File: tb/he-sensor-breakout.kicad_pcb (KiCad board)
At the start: 2 copper layers, 19 x 19 mm, 24 parts, among them J1 Conn_01x01_Pin, J10 Conn_01x01_Pin, J11 Conn_01x01_Pin, J12 Conn_01x01_Pin, J13 Conn_01x01_Pin, J14 Conn_01x01_Pin, J2 Conn_01x01_Pin, J3 Conn_01x01_Pin, J4 Conn_01x01_Pin, J5 Conn_01x01_Pin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

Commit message: adds panelization tabs
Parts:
- added REF**: Tab, kikit:Tab, F.Cu at (116.0, 107.8)
- added REF**: Tab, kikit:Tab, F.Cu at (111.0, 92.0)
- added REF**: Tab, kikit:Tab, F.Cu at (101.0, 114.0)
- added REF**: Tab, kikit:Tab, F.Cu at (111.0, 114.0)
- added REF**: Tab, kikit:Tab, F.Cu at (101.0, 92.0)
- added REF**: Tab, kikit:Tab, F.Cu at (116.0, 98.4)
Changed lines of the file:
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@@
     )
+  )
+  (footprint "kikit:Tab" (layer "F.Cu")
+    (at 116 107.7875 180)
+    (descr "A symbol representing annotation for tab placement")
+    (attr exclude_from_pos_files exclude_from_bom)
+    (fp_text reference "REF**" (at 0 -2) (layer "F.SilkS") hide
+        (effects (font (size 1 1) (thickness 0.15)))
+    )
+    (fp_text value "Tab" (at -3 -1) (layer "Dwgs.User")
+        (effects (font (size 1.2 1.2) (thickness 0.2)))
+    )
+    (fp_text user "KIKIT: width: 7mm" (at -5.5 0 90) (layer "Dwgs.User")
+        (effects (font (size 1 1) (thickness 0.15)))
+    )
+    (fp_line (start 0.25 0) (end -2.75 0)
+      (stroke (width 0.3) (type solid)) (layer "Dwgs.User"))
+    (fp_line (start 0.25 0) (end -0.75 -1)
+      (stroke (width 0.3) (type solid)) (layer "Dwgs.User"))
+    (fp_line (start 0.25 0) (end -0.75 1)
+      (stroke (width 0.3) (type solid)) (layer "Dwgs.User"))
+    (fp_line (start 0.25 1) (end 0.25 -1)
+      (stroke (width 0.3) (type solid)) (layer "Dwgs.User"))
+  )
+  (footprint "kikit:Tab" (layer "F.Cu")
+    (at 111 92 -90)
+    (descr "A symbol representing annotation for tab placement")
+    (attr exclude_from_pos_files exclude_from_bom)
+    (fp_text reference "REF**" (at 0 -2 90) (layer "F.SilkS") hide
+        (effects (font (size 1 1) (thickness 0.15)))
+    )
+    (fp_text value "Tab" (at -3 -1 90) (layer "Dwgs.User")
+        (effects (font (size 1.2 1.2) (thickness 0.2)))
+    )
+    (fp_text user "KIKIT: width: 3mm" (at -5.5 0) (layer "Dwgs.User")
+        (effects (font (size 1 1) (thickness 0.15)))
+    )
+    (fp_line (start 0.25 0) (end -2.75 0)
+      (stroke (width 0.3) (type solid)) (layer "Dwgs.User"))
+    (fp_line (start 0.25 0) (end -0.75 -1)
+      (stroke (width 0.3) (type solid)) (layer "Dwgs.User"))
+    (fp_line (start 0.25 0) (end -0.75 1)
+      (stroke (width 0.3) (type solid)) (layer "Dwgs.User"))
+    (fp_line (start 0.25 1) (end 0.25 -1)
+      (stroke (width 0.3) (type solid)) (layer "Dwgs.User"))
+  )
+  (footprint "kikit:Tab" (layer "F.Cu")
+    (at 101 114 90)
+    (descr "A symbol representing annotation for tab placement")
+    (attr exclude_from_pos_files exclude_from_bom)
+    (fp_text reference "REF**" (at 0 -2 90) (layer "F.SilkS") hide
+        (effects (font (size 1 1) (thickness 0.15)))
+    )
+    (fp_text value "Tab" (at -3 -1 90) (layer "Dwgs.User")
+        (effects (font (size 1.2 1.2) (thickness 0.2)))
+    )
+    (fp_text user "KIKIT: width: 3mm" (at -5.5 0) (layer "Dwgs.User")
+        (effects (font (size 1 1) (thickness 0.15)))
+    )
+    (fp_line (start 0.25 0) (end -2.75 0)
+      (stroke (width 0.3) (type solid)) (layer "Dwgs.User"))
+    (fp_line (start 0.25 0) (end -0.75 -1)
+      (stroke (width 0.3) (type solid)) (layer "Dwgs.User"))
+    (fp_line (start 0.25 0) (end -0.75 1)
+      (stroke (width 0.3) (type solid)) (layer "Dwgs.User"))
+    (fp_line (start 0.25 1) (end 0.25 -1)
+      (stroke (width 0.3) (type solid)) (layer "Dwgs.User"))
+  )
+  (footprint "kikit:Tab" (layer "F.Cu")
+    (at 111 114 90)
+    (descr "A symbol representing annotation for tab placement")
+    (attr exclude_from_pos_files exclude_from_bom)
+    (fp_text reference "REF**" (at 0 -2 90) (layer "F.SilkS") hide
+        (effects (font (size 1 1) (thickness 0.15)))
+    )
+    (fp_text value "Tab" (at -3 -1 90) (layer "Dwgs.User")
+        (effects (font (size 1.2 1.2) (thickness 0.2)))
+    )
+    (fp_text user "KIKIT: width: 3mm" (at -5.5 0) (layer "Dwgs.User")
+        (effects (font (size 1 1) (thickness 0.15)))
+    )
+    (fp_line (start 0.25 0) (end -2.75 0)
+      (stroke (width 0.3) (type solid)) (layer "Dwgs.User"))
+    (fp_line (start 0.25 0) (end -0.75 -1)
+      (stroke (width 0.3) (type solid)) (layer "Dwgs.User"))
+    (fp_line (start 0.25 0) (end -0.75 1)
+      (stroke (width 0.3) (type solid)) (layer "Dwgs.User"))
+    (fp_line (start 0.25 1) (end 0.25 -1)
+      (stroke (width 0.3) (type solid)) (layer "Dwgs.User"))
+  )
+  (footprint "kikit:Tab" (layer "F.Cu")
+    (at 101 92 -90)
+    (descr "A symbol representing annotation for tab placement")
+    (attr exclude_from_pos_files exclude_from_bom)
+    (fp_text reference "REF**" (at 0 -2 90) (layer "F.SilkS") hide
+        (effects (font (size 1 1) (thickness 0.15)))
+    )
+    (fp_text value "Tab" (at -3 -1 90) (layer "Dwgs.User")
+        (effects (font (size 1.2 1.2) (thickness 0.2)))
+    )
+    (fp_text user "KIKIT: width: 3mm" (at -5.5 0) (layer "Dwgs.User")
+        (effects (font (size 1 1) (thickness 0.15)))
+    )
+    (fp_line (start 0.25 0) (end -2.75 0)
+      (stroke (width 0.3) (type solid)) (layer "Dwgs.User"))
+    (fp_line (start 0.25 0) (end -0.75 -1)
+      (stroke (width 0.3) (type solid)) (layer "Dwgs.User"))
+    (fp_line (start 0.25 0) (end -0.75 1)
+      (stroke (width 0.3) (type solid)) (layer "Dwgs.User"))
+    (fp_line (start 0.25 1) (end 0.25 -1)
+      (stroke (width 0.3) (type solid)) (layer "Dwgs.User"))
+  )
+  (footprint "kikit:Tab" (layer "F.Cu")
+    (at 116 98.4125 180)
+    (descr "A symbol representing annotation for tab placement")
+    (attr exclude_from_pos_files exclude_from_bom)
+    (fp_text reference "REF**" (at 0 -2) (layer "F.SilkS") hide
+        (effects (font (size 1 1) (thickness 0.15)))
+    )
+    (fp_text value "Tab" (at -3 -1) (layer "Dwgs.User")
+        (effects (font (size 1.2 1.2) (thickness 0.2)))
+    )
+    (fp_text user "KIKIT: width: 7mm" (at -5.5 0 90) (layer "Dwgs.User")
+        (effects (font (size 1 1) (thickness 0.15)))
+    )
+    (fp_line (start 0.25 0) (end -2.75 0)
+      (stroke (width 0.3) (type solid)) (layer "Dwgs.User"))
+    (fp_line (start 0.25 0) (end -0.75 -1)
+      (stroke (width 0.3) (type solid)) (layer "Dwgs.User"))
+    (fp_line (start 0.25 0) (end -0.75 1)
+      (stroke (width 0.3) (type solid)) (layer "Dwgs.User"))
+    (fp_line (start 0.25 1) (end 0.25 -1)
+      (stroke (width 0.3) (type solid)) (layer "Dwgs.User"))
   )
   (footprint "Resistor_SMD:R_0402_1005Metric_Pad0.72x0.64mm_HandSolder" (layer "B.Cu")
@@
   (zone (net 3) (net_name "GNDD") (layer "F.Cu") (hatch edge 0.5)
     (priority 1)
-    (connect_pads (clearance 0))
+    (connect_pads (clearance 0.5))
     (min_thickness 0.25) (filled_areas_thickness no)
     (fill yes (thermal_gap 0.5) (thermal_bridge_width 0.5))

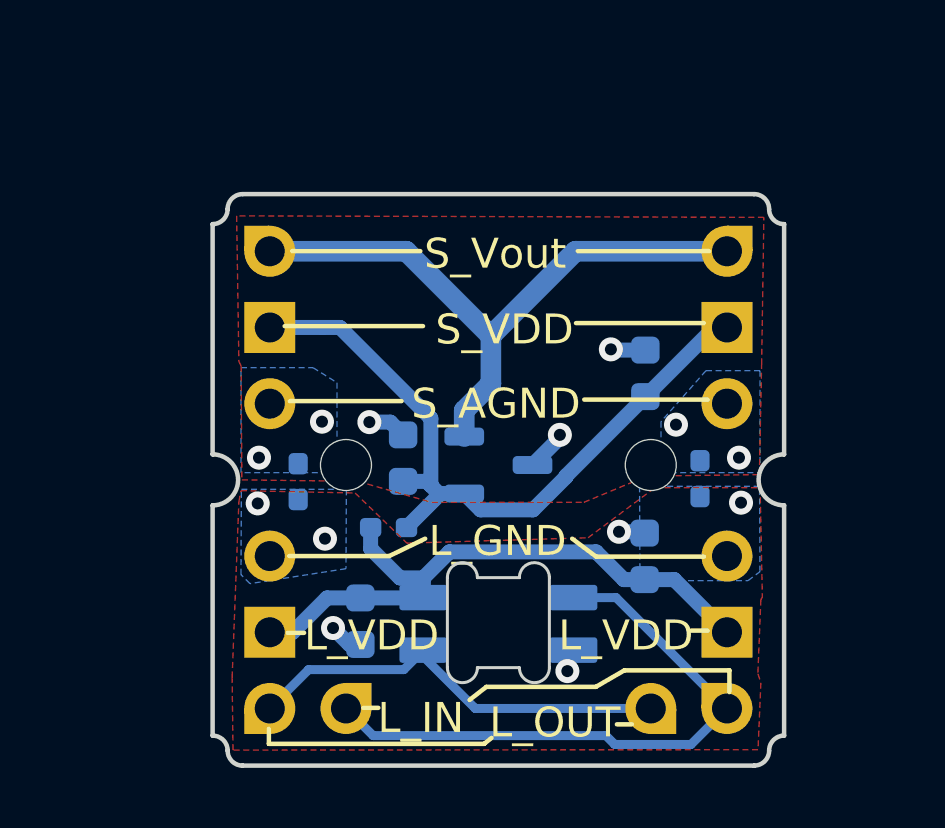
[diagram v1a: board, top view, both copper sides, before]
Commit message: changes tabs
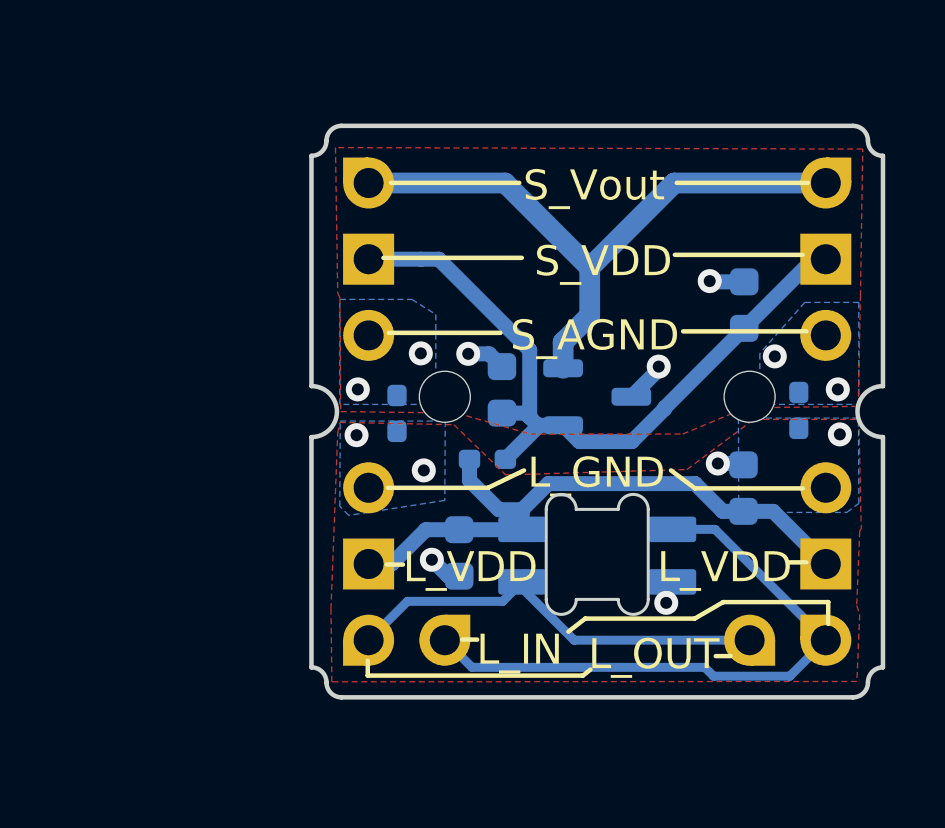
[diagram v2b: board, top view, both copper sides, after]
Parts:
- removed the REF** at (101.0, 114.0)
- removed the REF** at (101.0, 92.0)
- moved C1 4.00 mm to (104.6, 105.5)
- moved C2 4.00 mm to (114.1, 103.4)
- moved C4 4.00 mm to (106.0, 100.1)
- moved D1 4.00 mm to (109.2, 105.6)
- moved J1 4.00 mm to (116.8, 105.9)
- moved J4 4.00 mm to (116.8, 98.3)
- moved J7 4.00 mm to (116.8, 103.4)
- moved J9 4.00 mm to (116.8, 93.2)
- moved R1 4.00 mm to (115.9, 100.8)
- moved SW 4.00 mm to (109.2, 100.3)
- moved U1 4.00 mm to (109.2, 100.3)
- moved C3 4.00 mm to (114.1, 97.3)
- moved J11 4.00 mm to (114.3, 108.4)
- moved J13 4.00 mm to (104.1, 108.4)
- moved J14 4.00 mm to (116.8, 108.4)
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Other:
- board size 19 x 19 mm -> 19.1 x 19 mm

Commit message: shrink 1x1 and add 2u outline
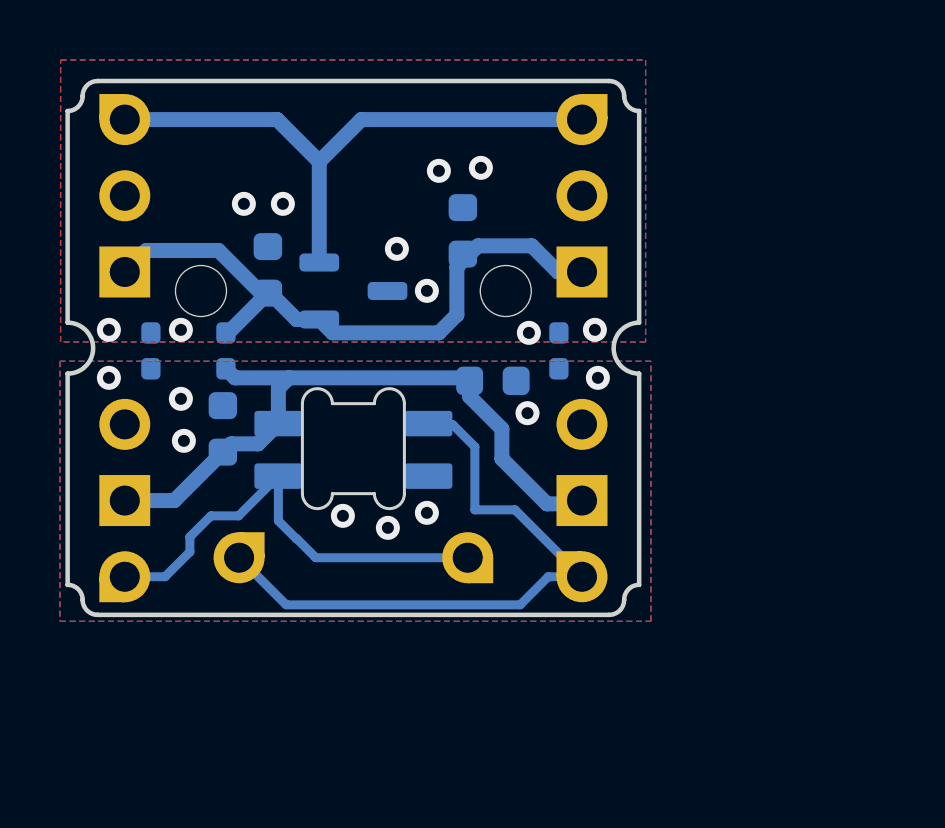
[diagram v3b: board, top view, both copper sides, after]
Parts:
- moved REF** 17.9 mm to (137.2, 96.5)
- moved REF** 17.9 mm to (137.2, 105.5)
- moved REF** 12.7 mm to (109.2, 124.5)
- moved J11 9.79 mm to (104.9, 105.7)
- moved C3 9.70 mm to (104.7, 94.8)
- moved R3 9.44 mm to (96.8, 98.8), turned to 90 degrees
- moved J3 9.37 mm to (93.5, 93.6)
- moved J4 9.37 mm to (108.7, 93.6)
- moved C2 9.09 mm to (105.7, 99.8), turned to 180 degrees
- moved C1 8.90 mm to (96.7, 101.4), turned to -90 degrees
- moved REF** 8.89 mm to (109.2, 81.3)
- moved D1 8.86 mm to (101.1, 102.1)
- moved SW 8.86 mm to (101.1, 96.8)
- moved U1 8.86 mm to (101.1, 96.8)
- moved C4 8.77 mm to (98.2, 96.1)
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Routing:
- net GNDA: track 3.84 -> 0.00 mm, vias 7 -> 10
- net VDDA: track 24.6 -> 21.1 mm
- net GNDD: track 2.80 -> 0.00 mm, vias 6 -> 8
- net VDD: track 20.7 -> 22.5 mm
- net Vout: track 21.3 -> 19.8 mm
- net LED_OUT: track 14.4 -> 15.3 mm
- net LED_IN: track 20.3 -> 20.9 mm
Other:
- board size 19.1 x 19 mm -> 19.1 x 17.8 mm
- board text removed: "L_GND"
- board text removed: "L_IN"
- board text removed: "L_OUT"
- board text removed: "L_VDD"
- board text removed: "S_AGND"
- board text removed: "S_VDD"
- board text removed: "S_Vout"

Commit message: fixes kikit tabs
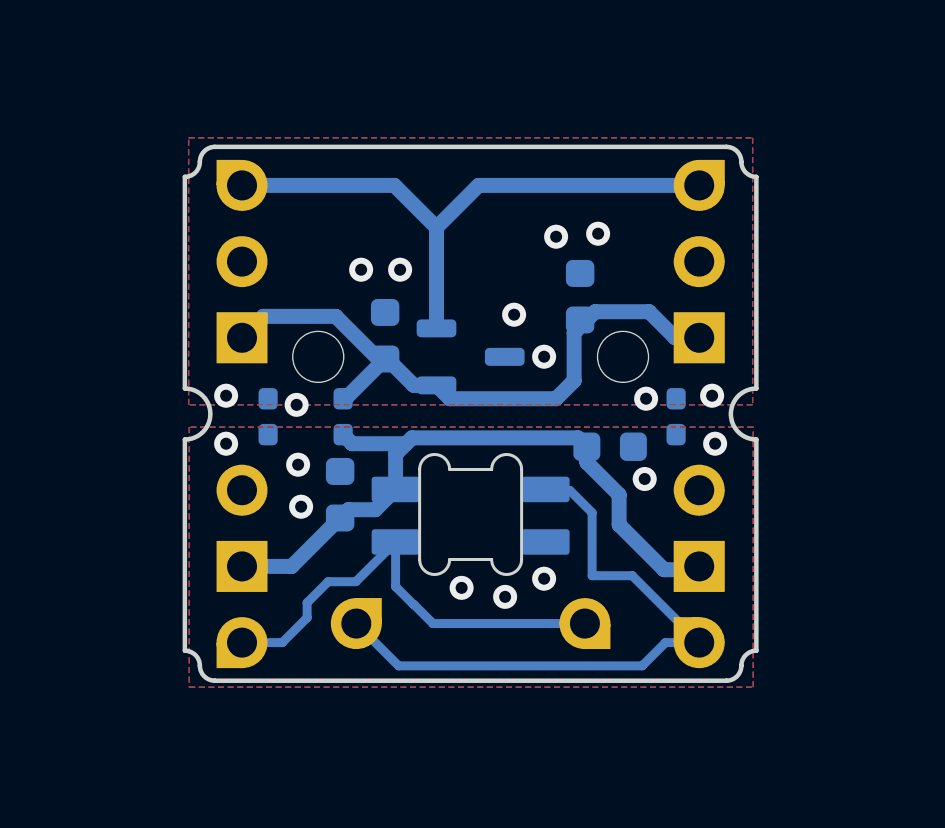
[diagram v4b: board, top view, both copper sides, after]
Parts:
- moved REF** 21.2 mm to (116.0, 105.3)
- moved REF** 21.2 mm to (116.0, 96.5)
- moved REF** 14.1 mm to (105.0, 111.0)
- moved REF** 10.6 mm to (105.0, 91.0)
- moved C2 4.48 mm to (109.7, 102.0)
- moved C3 4.48 mm to (108.7, 97.0)
- moved C4 4.48 mm to (102.2, 98.3)
- moved D1 4.48 mm to (105.0, 104.3)
- moved J11 4.48 mm to (108.8, 107.9)
- moved J12 4.48 mm to (97.4, 108.5)
- moved J13 4.48 mm to (101.2, 107.9)
- moved J14 4.48 mm to (112.6, 108.5)
- moved J3 4.48 mm to (97.4, 95.8)
- moved J4 4.48 mm to (112.6, 95.8)
- moved R1 4.48 mm to (111.8, 101.0)
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
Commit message: adds silkscreen to 1x1
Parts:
- moved C1 4.28 mm to (104.9, 104.3)
- moved J1 4.28 mm to (116.8, 106.7)
- moved J10 4.28 mm to (101.6, 94.0)
- moved J2 4.28 mm to (101.6, 106.7)
- moved J5 4.28 mm to (101.6, 99.1)
- moved J6 4.28 mm to (116.8, 99.1)
- moved J7 4.28 mm to (116.8, 104.1)
- moved J8 4.28 mm to (101.6, 104.1)
- moved J9 4.28 mm to (116.8, 94.0)
- moved C2 4.28 mm to (113.9, 102.7)
- moved C3 4.28 mm to (112.9, 97.7)
- moved C4 4.28 mm to (106.4, 99.0)
- moved D1 4.28 mm to (109.2, 105.0)
- moved J11 4.28 mm to (113.0, 108.6)
- moved J12 4.28 mm to (101.6, 109.2)
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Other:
- board text added: "LVDD"
- board text added: "L_GND"
- board text added: "L_IN"
- board text added: "L_OUT"
- board text added: "L_VDD"
- board text added: "S_GND"
- board text added: "S_VDD"
- board text added: "Vout"

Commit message: make symmetric
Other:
- outline, holes or cut-outs redrawn
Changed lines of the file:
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@@
   (gr_arc (start 118.745026 103.6) (mid 116.745 101.6) (end 118.745026 99.6)
     (stroke (width 0.15) (type default)) (layer "Dwgs.User"))
-  (gr_arc (start 100.195 93.195) (mid 100.048553 93.548553) (end 99.695 93.695)
+  (gr_arc (start 100.195 93.21) (mid 100.048553 93.563553) (end 99.695 93.71)
     (stroke (width 0.15) (type default)) (layer "Edge.Cuts"))
   (gr_arc (start 118.745 102.45) (mid 117.895 101.6) (end 118.745 100.75)
     (stroke (width 0.15) (type default)) (layer "Edge.Cuts"))
-  (gr_line (start 99.695 93.695) (end 99.695 100.75)
+  (gr_line (start 99.695 93.71) (end 99.695 100.765)
     (stroke (width 0.15) (type default)) (layer "Edge.Cuts"))
   (gr_line (start 117.745 110.49) (end 100.695 110.49)
@@
   (gr_line (start 118.745 102.45) (end 118.745 109.49)
     (stroke (width 0.15) (type default)) (layer "Edge.Cuts"))
-  (gr_line (start 118.745 93.695) (end 118.745 100.75)
+  (gr_line (start 118.745 93.71) (end 118.745 100.75)
     (stroke (width 0.15) (type default)) (layer "Edge.Cuts"))
   (gr_line (start 99.695 102.45) (end 99.695 109.49)
@@
   (gr_arc (start 99.695 100.75) (mid 100.545 101.6) (end 99.695 102.45)
     (stroke (width 0.15) (type default)) (layer "Edge.Cuts"))
-  (gr_line (start 100.695 92.695) (end 117.745 92.695)
+  (gr_line (start 100.695 92.71) (end 117.745 92.71)
     (stroke (width 0.15) (type default)) (layer "Edge.Cuts"))
-  (gr_arc (start 100.195 93.195) (mid 100.341447 92.841447) (end 100.695 92.695)
+  (gr_arc (start 100.195 93.21) (mid 100.341447 92.856447) (end 100.695 92.71)
     (stroke (width 0.15) (type default)) (layer "Edge.Cuts"))
   (gr_arc (start 118.245 109.99) (mid 118.098612 110.343612) (end 117.745 110.49)
     (stroke (width 0.15) (type default)) (layer "Edge.Cuts"))
-  (gr_arc (start 117.745 92.695) (mid 118.098553 92.841447) (end 118.245 93.195)
+  (gr_arc (start 117.745 92.71) (mid 118.098553 92.856447) (end 118.245 93.21)
     (stroke (width 0.15) (type default)) (layer "Edge.Cuts"))
   (gr_arc (start 99.695 109.49) (mid 100.048553 109.636447) (end 100.195 109.99)
     (stroke (width 0.15) (type default)) (layer "Edge.Cuts"))
-  (gr_arc (start 118.745 93.695) (mid 118.391447 93.548553) (end 118.245 93.195)
+  (gr_arc (start 118.745 93.71) (mid 118.391447 93.563553) (end 118.245 93.21)
     (stroke (width 0.15) (type default)) (layer "Edge.Cuts"))
   (gr_arc (start 100.695 110.49) (mid 100.341447 110.343553) (end 100.195 109.99)
